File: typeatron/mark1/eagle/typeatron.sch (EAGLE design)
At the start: 26 parts

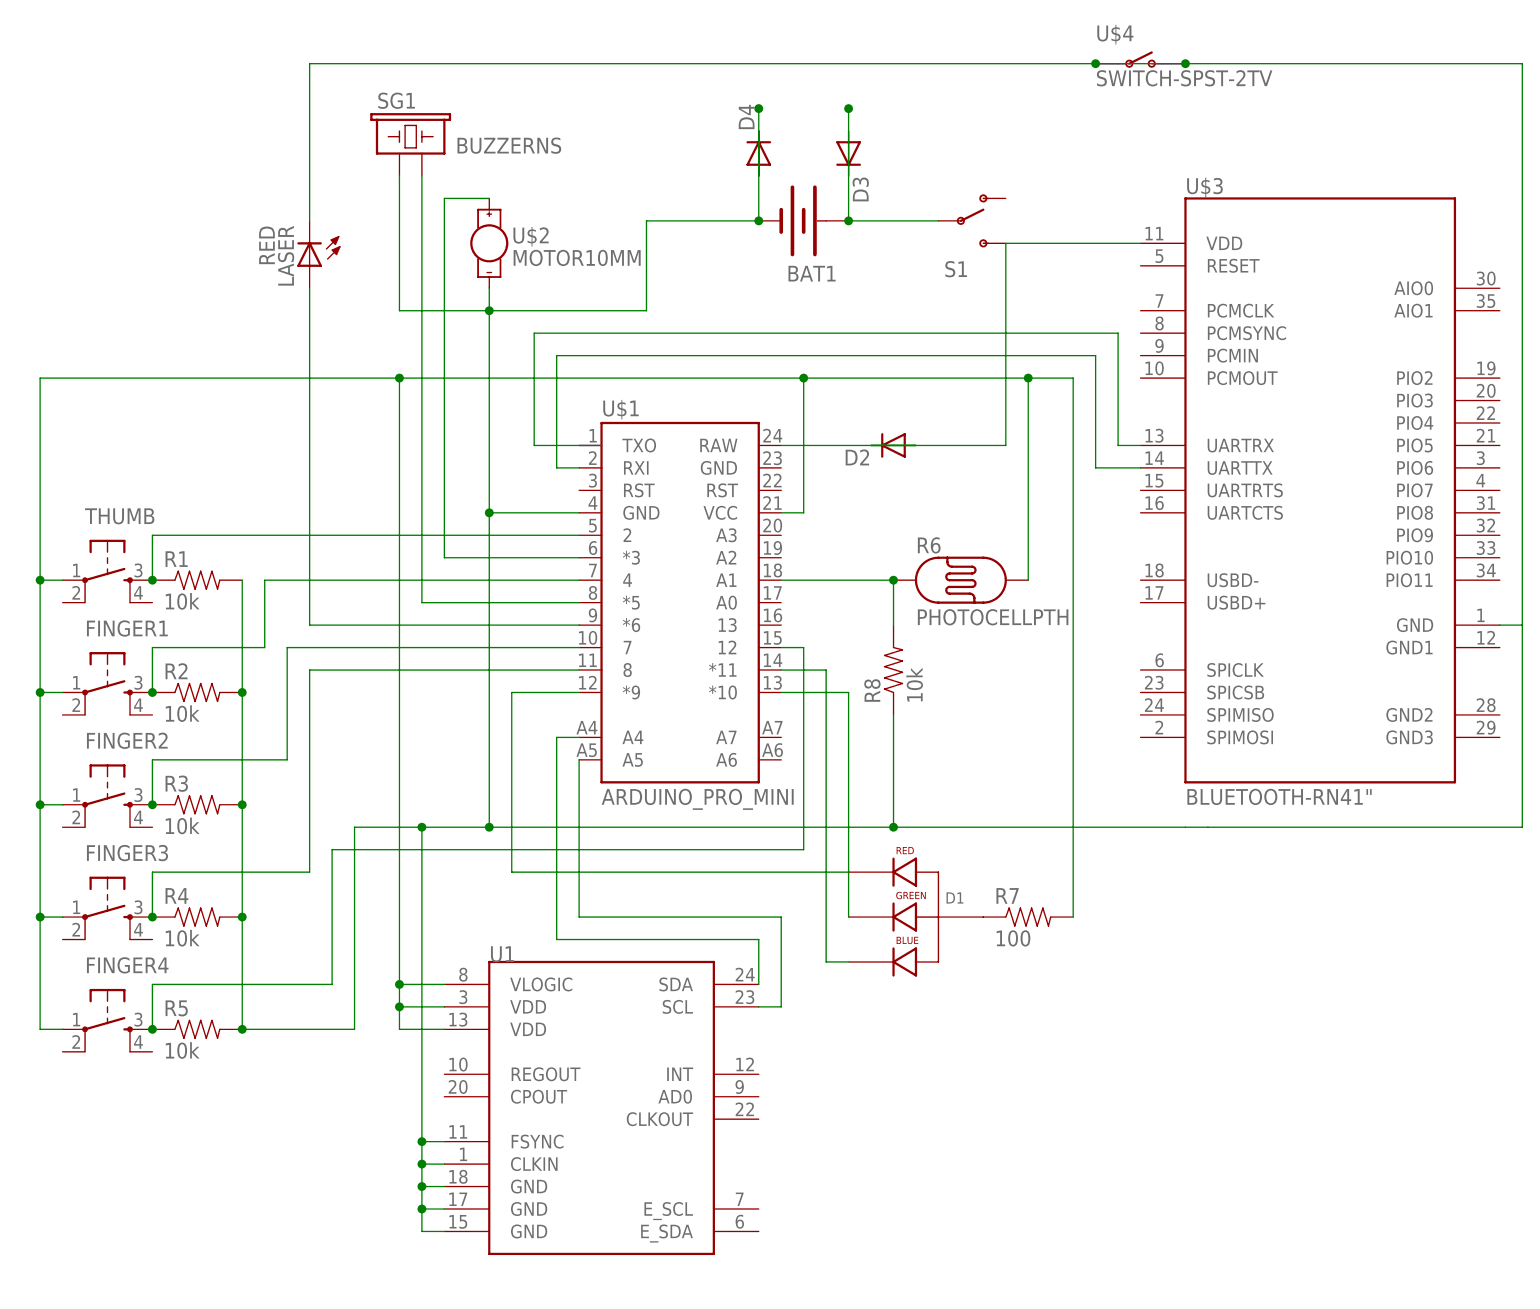
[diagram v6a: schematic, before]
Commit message: Minor tweaks to Typeatron wiring
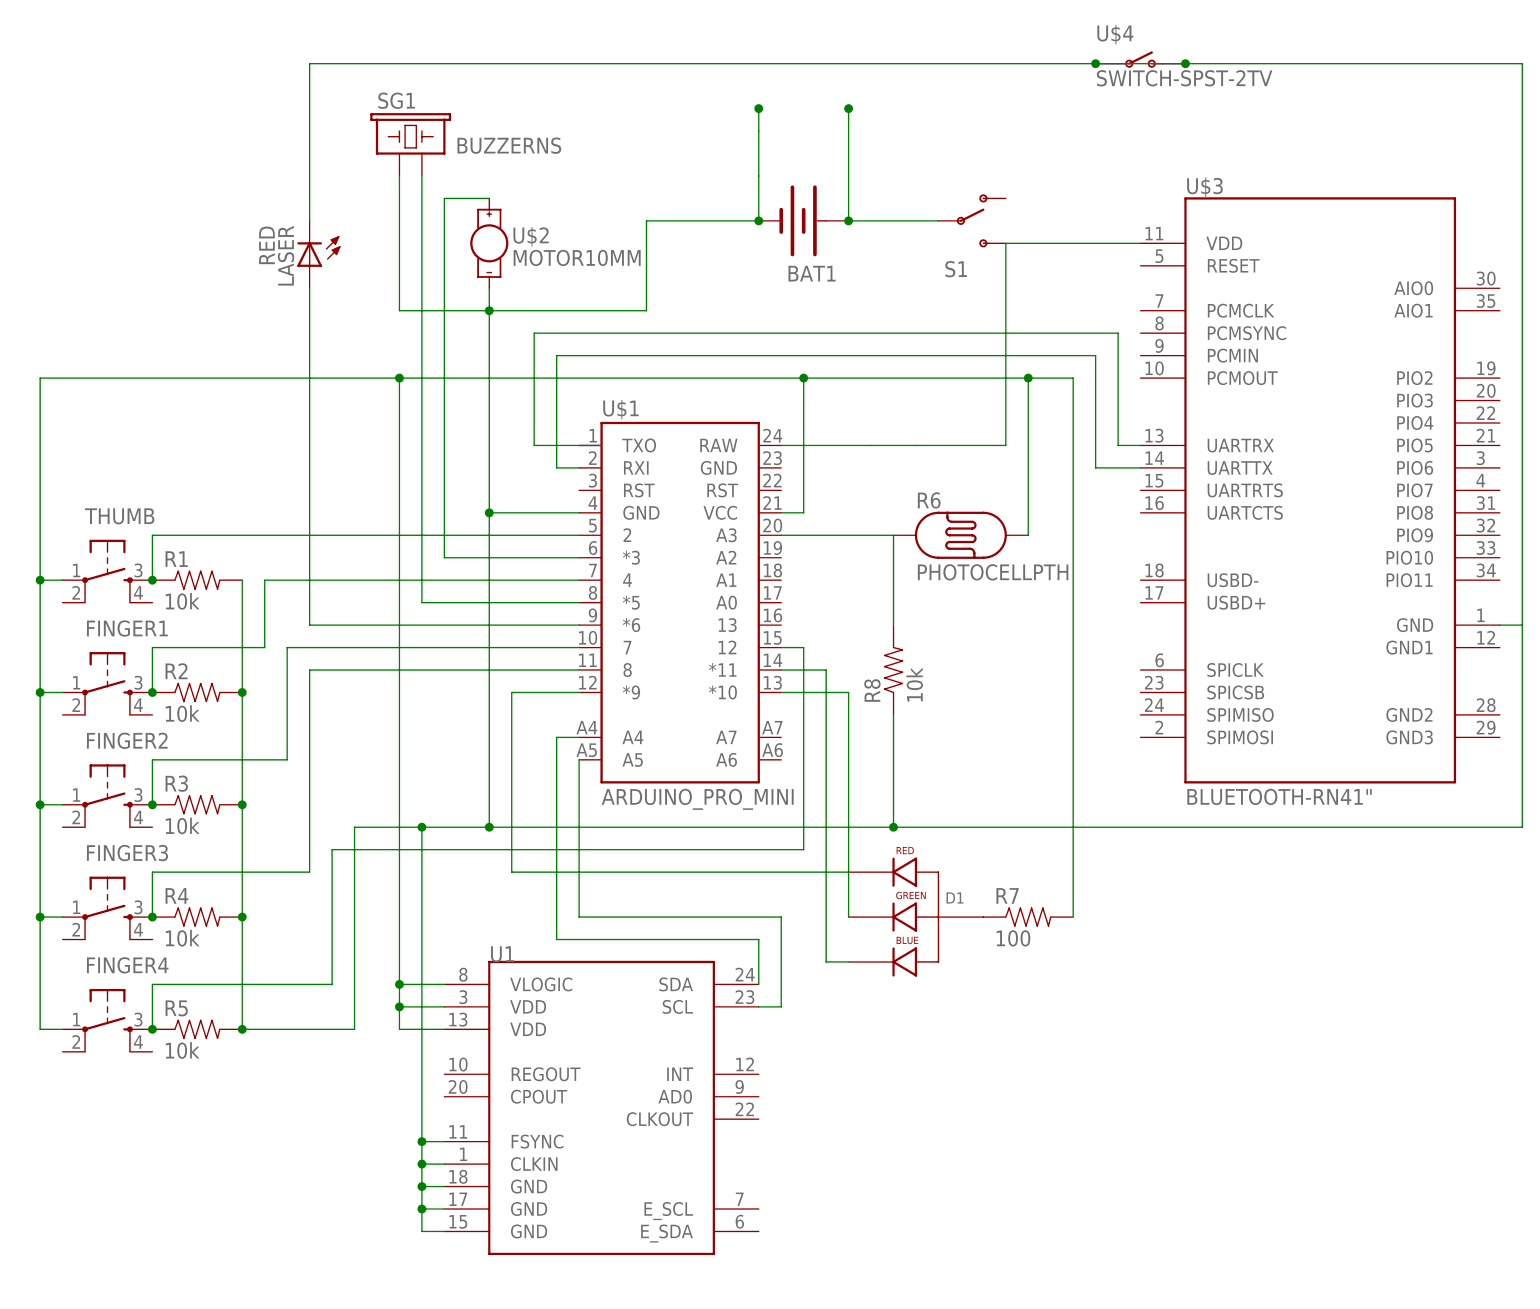
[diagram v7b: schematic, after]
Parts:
- removed D2, D3, D4: (no value), SparkFun-DiscreteSemi:DIODEPTH
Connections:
- removed net N$9: BAT1.+, D3.A, D3.C, S1.P
- new net N$24: BAT1.+, S1.P
- net N$10: no longer D2.A, D2.C
- net N$3: no longer D4.A, D4.C
- net N$8: now also U$1.A3; no longer U$1.A1
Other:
- moved on the sheet: R6
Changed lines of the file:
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@@
 <part name="U1" library="SparkFun-Sensors" deviceset="MPU-9150" device="QFN-24-NP"/>
 <part name="R8" library="SparkFun-Resistors" deviceset="10KOHM1/6W5%(PTH)" device="KIT" value="10k"/>
-<part name="D2" library="SparkFun-DiscreteSemi" deviceset="DIODE" device="PTH"/>
 <part name="LASER" library="SparkFun-LED" deviceset="LED-RED" device="0603" value="RED"/>
-<part name="D3" library="SparkFun-DiscreteSemi" deviceset="DIODE" device="PTH"/>
-<part name="D4" library="SparkFun-DiscreteSemi" deviceset="DIODE" device="PTH"/>
 <part name="U$4" library="SparkFun-Electromechanical" deviceset="SWITCH-SPST-2" device="TV"/>
 </parts>
@@
 <instance part="U$3" gate="G$1" x="134.62" y="76.2"/>
 <instance part="BAT1" gate="G$1" x="76.2" y="106.68" rot="R180"/>
-<instance part="R6" gate="G$1" x="93.98" y="66.04"/>
+<instance part="R6" gate="G$1" x="93.98" y="71.12"/>
 <instance part="D1" gate="G$1" x="86.36" y="27.94"/>
 <instance part="R7" gate="G$1" x="101.6" y="27.94"/>
 <instance part="U1" gate="G$1" x="53.34" y="5.08"/>
 <instance part="R8" gate="G$1" x="86.36" y="55.88" rot="R90"/>
-<instance part="D2" gate="G$1" x="86.36" y="81.28" rot="R180"/>
 <instance part="LASER" gate="G$1" x="20.32" y="101.6" rot="R180"/>
-<instance part="D3" gate="G$1" x="81.28" y="114.3" rot="R270"/>
-<instance part="D4" gate="G$1" x="71.12" y="114.3" rot="R90"/>
 <instance part="U$4" gate="G$1" x="114.3" y="124.46"/>
 </instances>
@@
 <pinref part="R6" gate="G$1" pin="P$1"/>
 <pinref part="R8" gate="G$1" pin="2"/>
-<wire x1="86.36" y1="60.96" x2="86.36" y2="66.04" width="0.1524" layer="91"/>
-<pinref part="U$1" gate="G$1" pin="A1"/>
-<wire x1="73.66" y1="66.04" x2="86.36" y2="66.04" width="0.1524" layer="91"/>
-<junction x="86.36" y="66.04"/>
+<wire x1="86.36" y1="60.96" x2="86.36" y2="71.12" width="0.1524" layer="91"/>
+<pinref part="U$1" gate="G$1" pin="A3"/>
+<wire x1="86.36" y1="71.12" x2="73.66" y2="71.12" width="0.1524" layer="91"/>
 </segment>
 </net>
@@
 <wire x1="76.2" y1="88.9" x2="101.6" y2="88.9" width="0.1524" layer="91"/>
 <wire x1="101.6" y1="88.9" x2="106.68" y2="88.9" width="0.1524" layer="91"/>
-<wire x1="101.6" y1="66.04" x2="101.6" y2="88.9" width="0.1524" layer="91"/>
+<wire x1="101.6" y1="71.12" x2="101.6" y2="88.9" width="0.1524" layer="91"/>
 <junction x="101.6" y="88.9"/>
 <pinref part="R7" gate="G$1" pin="2"/>
@@
 </segment>
 </net>
-<net name="N$9" class="0">
-<segment>
-<pinref part="BAT1" gate="G$1" pin="+"/>
-<pinref part="S1" gate="1" pin="P"/>
-<wire x1="81.28" y1="119.38" x2="81.28" y2="116.84" width="0.1524" layer="91"/>
-<junction x="81.28" y="106.68"/>
-<wire x1="81.28" y1="116.84" x2="81.28" y2="111.76" width="0.1524" layer="91"/>
-<wire x1="81.28" y1="111.76" x2="81.28" y2="106.68" width="0.1524" layer="91"/>
-<wire x1="81.28" y1="106.68" x2="91.44" y2="106.68" width="0.1524" layer="91"/>
-<junction x="81.28" y="119.38"/>
-<pinref part="D3" gate="G$1" pin="A"/>
-<pinref part="D3" gate="G$1" pin="C"/>
-</segment>
-</net>
 <net name="N$10" class="0">
 <segment>
 <pinref part="S1" gate="1" pin="S"/>
 <pinref part="U$1" gate="G$1" pin="RAW"/>
-<wire x1="73.66" y1="81.28" x2="88.9" y2="81.28" width="0.1524" layer="91"/>
+<wire x1="73.66" y1="81.28" x2="83.82" y2="81.28" width="0.1524" layer="91"/>
 <wire x1="88.9" y1="81.28" x2="83.82" y2="81.28" width="0.1524" layer="91"/>
-<wire x1="83.82" y1="81.28" x2="99.06" y2="81.28" width="0.1524" layer="91"/>
+<wire x1="88.9" y1="81.28" x2="99.06" y2="81.28" width="0.1524" layer="91"/>
 <wire x1="99.06" y1="81.28" x2="99.06" y2="104.14" width="0.1524" layer="91"/>
 <pinref part="U$3" gate="G$1" pin="VDD"/>
-<pinref part="D2" gate="G$1" pin="A"/>
-<pinref part="D2" gate="G$1" pin="C"/>
 <wire x1="99.06" y1="104.14" x2="114.3" y2="104.14" width="0.1524" layer="91"/>
 </segment>
@@
 <wire x1="40.64" y1="73.66" x2="40.64" y2="38.1" width="0.1524" layer="91"/>
 <wire x1="33.02" y1="2.54" x2="33.02" y2="38.1" width="0.1524" layer="91"/>
-<wire x1="86.36" y1="38.1" x2="119.38" y2="38.1" width="0.1524" layer="91"/>
 <pinref part="SG1" gate="G$1" pin="1"/>
 <wire x1="30.48" y1="111.76" x2="30.48" y2="96.52" width="0.1524" layer="91"/>
@@
 <wire x1="40.64" y1="96.52" x2="58.42" y2="96.52" width="0.1524" layer="91"/>
 <pinref part="BAT1" gate="G$1" pin="-"/>
-<wire x1="71.12" y1="119.38" x2="71.12" y2="111.76" width="0.1524" layer="91"/>
+<wire x1="71.12" y1="119.38" x2="71.12" y2="116.84" width="0.1524" layer="91"/>
 <junction x="71.12" y="106.68"/>
 <wire x1="71.12" y1="111.76" x2="71.12" y2="116.84" width="0.1524" layer="91"/>
-<wire x1="71.12" y1="116.84" x2="71.12" y2="106.68" width="0.1524" layer="91"/>
+<wire x1="71.12" y1="111.76" x2="71.12" y2="106.68" width="0.1524" layer="91"/>
 <wire x1="71.12" y1="106.68" x2="58.42" y2="106.68" width="0.1524" layer="91"/>
 <wire x1="58.42" y1="96.52" x2="58.42" y2="106.68" width="0.1524" layer="91"/>
@@
 <wire x1="50.8" y1="73.66" x2="40.64" y2="73.66" width="0.1524" layer="91"/>
 <junction x="40.64" y="73.66"/>
-<pinref part="D4" gate="G$1" pin="A"/>
-<pinref part="D4" gate="G$1" pin="C"/>
 <pinref part="U$3" gate="G$1" pin="GND"/>
-<wire x1="119.38" y1="38.1" x2="121.92" y2="38.1" width="0.1524" layer="91"/>
-<wire x1="121.92" y1="38.1" x2="157.48" y2="38.1" width="0.1524" layer="91"/>
+<wire x1="86.36" y1="38.1" x2="157.48" y2="38.1" width="0.1524" layer="91"/>
 <wire x1="157.48" y1="38.1" x2="157.48" y2="60.96" width="0.1524" layer="91"/>
 <wire x1="157.48" y1="60.96" x2="154.94" y2="60.96" width="0.1524" layer="91"/>
@@
 </segment>
 </net>
+<net name="N$24" class="0">
+<segment>
+<junction x="81.28" y="119.38"/>
+<pinref part="BAT1" gate="G$1" pin="+"/>
+<pinref part="S1" gate="1" pin="P"/>
+<junction x="81.28" y="106.68"/>
+<wire x1="81.28" y1="106.68" x2="91.44" y2="106.68" width="0.1524" layer="91"/>
+<wire x1="81.28" y1="119.38" x2="81.28" y2="106.68" width="0.1524" layer="91"/>
+</segment>
+</net>

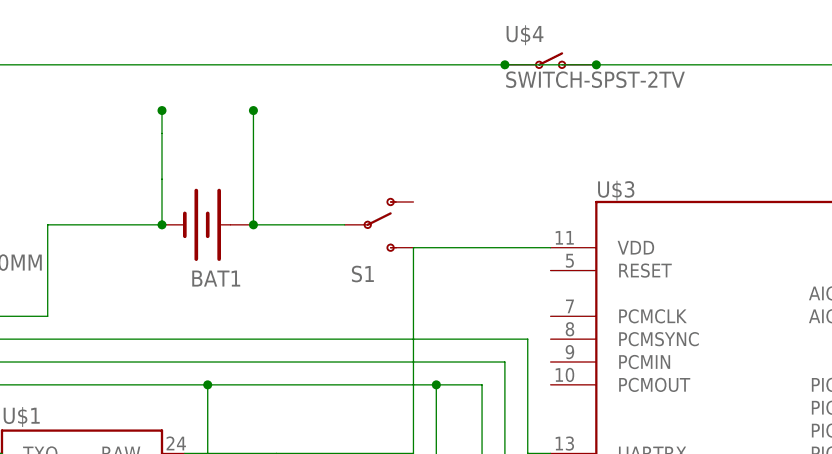
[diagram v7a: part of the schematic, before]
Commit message: Brainstem changes to support Android-->Arduino OSC messaging.  Also updated Typeatron schematic to match the completed prototype
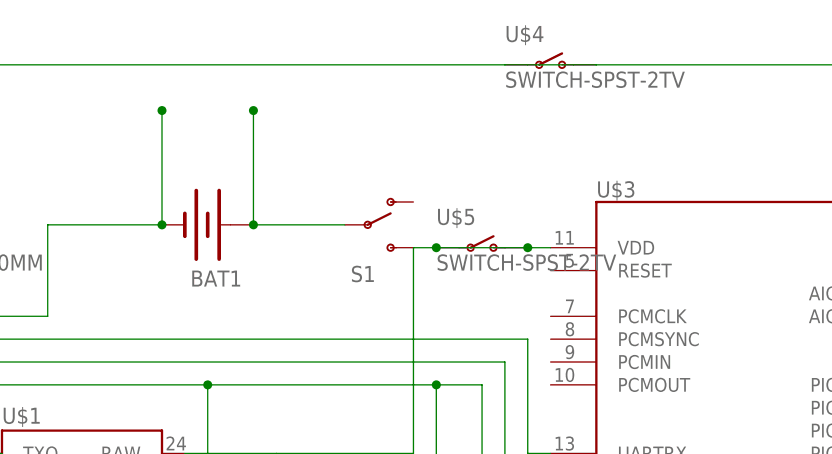
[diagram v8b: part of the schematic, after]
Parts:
- added U$5: SWITCH-SPST-2TV, SparkFun-Electromechanical:SWITCH-SPST-2TV
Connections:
- net N$10: now also U$5.O, U$5.P
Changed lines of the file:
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@@
 <part name="LASER" library="SparkFun-LED" deviceset="LED-RED" device="0603" value="RED"/>
 <part name="U$4" library="SparkFun-Electromechanical" deviceset="SWITCH-SPST-2" device="TV"/>
+<part name="U$5" library="SparkFun-Electromechanical" deviceset="SWITCH-SPST-2" device="TV"/>
 </parts>
 <sheets>
@@
 <instance part="LASER" gate="G$1" x="20.32" y="101.6" rot="R180"/>
 <instance part="U$4" gate="G$1" x="114.3" y="124.46"/>
+<instance part="U$5" gate="G$1" x="106.68" y="104.14"/>
 </instances>
 <busses>
@@
 <wire x1="99.06" y1="81.28" x2="99.06" y2="104.14" width="0.1524" layer="91"/>
 <pinref part="U$3" gate="G$1" pin="VDD"/>
-<wire x1="99.06" y1="104.14" x2="114.3" y2="104.14" width="0.1524" layer="91"/>
+<wire x1="99.06" y1="104.14" x2="101.6" y2="104.14" width="0.1524" layer="91"/>
+<pinref part="U$5" gate="G$1" pin="P"/>
+<wire x1="101.6" y1="104.14" x2="111.76" y2="104.14" width="0.1524" layer="91"/>
+<junction x="101.6" y="104.14"/>
+<pinref part="U$5" gate="G$1" pin="O"/>
+<wire x1="111.76" y1="104.14" x2="114.3" y2="104.14" width="0.1524" layer="91"/>
+<junction x="111.76" y="104.14"/>
 </segment>
 </net>
@@
 <wire x1="40.64" y1="96.52" x2="58.42" y2="96.52" width="0.1524" layer="91"/>
 <pinref part="BAT1" gate="G$1" pin="-"/>
-<wire x1="71.12" y1="119.38" x2="71.12" y2="116.84" width="0.1524" layer="91"/>
 <junction x="71.12" y="106.68"/>
-<wire x1="71.12" y1="111.76" x2="71.12" y2="116.84" width="0.1524" layer="91"/>
-<wire x1="71.12" y1="111.76" x2="71.12" y2="106.68" width="0.1524" layer="91"/>
+<wire x1="71.12" y1="119.38" x2="71.12" y2="106.68" width="0.1524" layer="91"/>
 <wire x1="71.12" y1="106.68" x2="58.42" y2="106.68" width="0.1524" layer="91"/>
 <wire x1="58.42" y1="96.52" x2="58.42" y2="106.68" width="0.1524" layer="91"/>
@@
 <wire x1="157.48" y1="124.46" x2="157.48" y2="60.96" width="0.1524" layer="91"/>
 <pinref part="U$4" gate="G$1" pin="P"/>
-<junction x="109.22" y="124.46"/>
 <pinref part="U$4" gate="G$1" pin="O"/>
-<junction x="119.38" y="124.46"/>
-</segment>
-</net>
+</segment>
+</net>
